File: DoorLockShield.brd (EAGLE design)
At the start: 160 x 100 mm, 1 part

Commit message: added schematic
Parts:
- added 24V: (no value), con-ptr500:AK500/2
- added C1: (no value), rcl:E7,5-16
- added FREI, L_V_T_N: (no value), con-phoenix-254:4POL254
- added IC2: 74HC595N, 74xx-eu:DIL16
- added L_V_T_O: (no value), con-phoenix-254:6POL254
- added RANDOM: (no value), con-phoenix-254:5POL254
- added RFID: (no value), con-phoenix-254:8POL254
- added RFID-LED: (no value), con-phoenix-254:3POL254
- added R_S_D, TT: (no value), con-phoenix-254:2POL254
- added SV1: (no value), con-lstb:MA03-1
- added SV2, SV3: (no value), con-lstb:MA08-1
- moved IC1 83.7 mm to (1.00, 6.08)
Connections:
- removed net +3V3: IC1.2
- new net 00: FREI.1, IC1.13
- new net 01: FREI.2, IC1.14
- new net 02: IC1.15, SV3.2
- new net 03: IC1.16, SV3.1
- new net 04: IC1.17
- new net 05: IC1.18, RFID.5
- new net 06: IC1.19
- new net 06_IN: RFID.4, SV1.2
- new net 07: IC1.20, IC2.14
- new net 08: IC1.21, IC2.12
- new net 09: IC1.22, IC2.11
- new net 10: IC1.23
- new net 11: IC1.24, RFID.3
- new net 12: IC1.25, RFID.2
- new net 13: IC1.26, RFID.1
- new net 1A: SV2.5
- new net 1B: SV2.6
- new net 24V: 24V.1, SV2.1
- new net 2A: SV2.4
- new net 2B: SV2.3
- new net 3.3V: IC1.2, RANDOM.3
- new net 5V: C1.+, IC1.6, IC2.10, IC2.16, L_V_T_N.3, L_V_T_O.4, RFID.6, SV1.3, SV2.7, SV3.6
- new net A0: IC1.7, L_V_T_O.2
- new net A1: IC1.8, R_S_D.2
- new net A2: L_V_T_O.1
- new net A3: IC1.10, TT.2
- new net A4: FREI.3, IC1.11
- new net A5: FREI.4, IC1.12
- new net AGND: C1.-, IC1.27, IC1.4, IC1.5, IC2.13, IC2.8, IC2.9, L_V_T_N.4, L_V_T_O.5, L_V_T_O.6, RFID.7, RFID.8, R_S_D.1, SV2.2, SV2.8, TT.1
- new net AREF: IC1.28, RANDOM.1
- new net N$1: SV1.1
- new net N$11: SV3.7
- new net N$13: SV3.5
- new net N$14: SV3.3, SV3.4
- new net N$6: IC2.7
- new net QA: IC2.15, RFID-LED.3
- new net QB: IC2.1, RFID-LED.2
- new net QC: IC2.2, RFID-LED.1
- new net QD: IC2.3, L_V_T_O.3
- new net QE: IC2.4, SV3.8
- new net QF: IC2.5, L_V_T_N.1
- new net QG: IC2.6, L_V_T_N.2
- new net RST: IC1.1, RANDOM.2
- net +5V: now also RANDOM.4
- net GND: now also 24V.2, RANDOM.5; no longer IC1.27, IC1.4, IC1.5
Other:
- board size 160 x 100 mm -> 70.6 x 65.4 mm

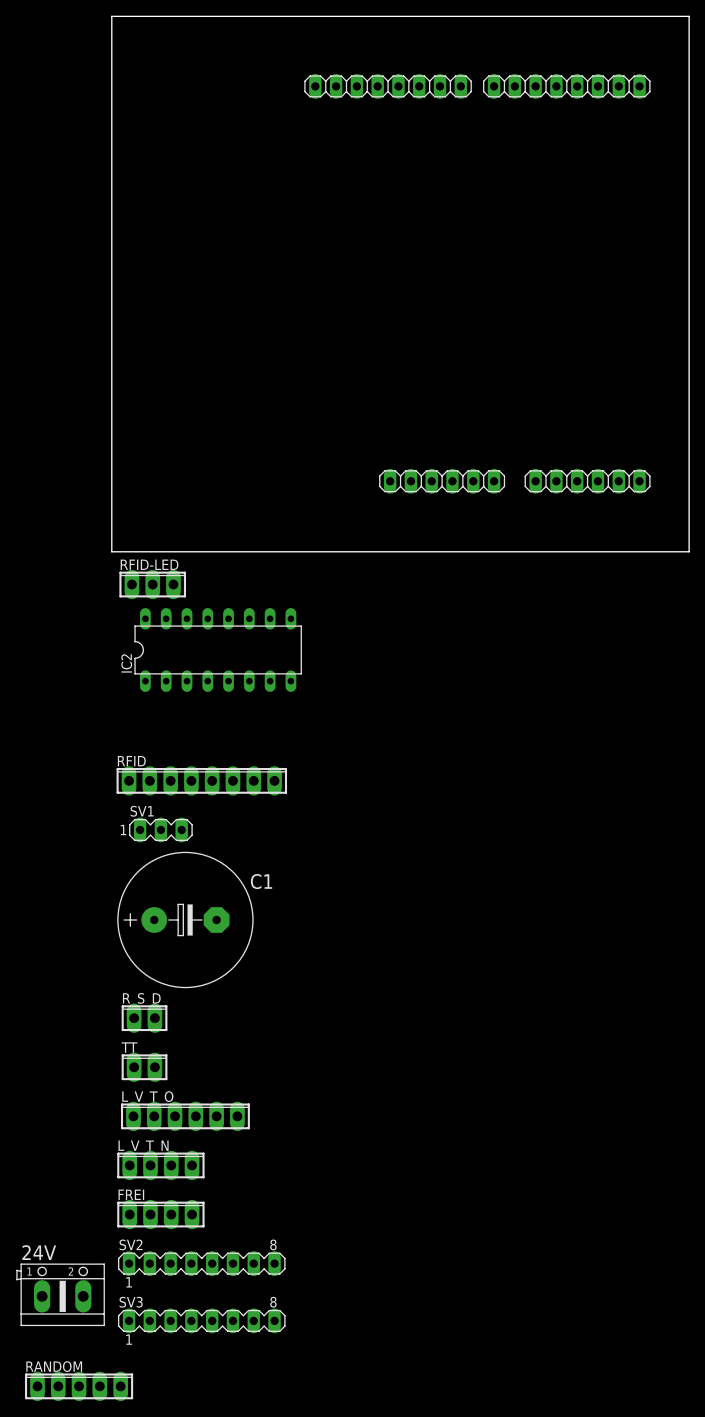
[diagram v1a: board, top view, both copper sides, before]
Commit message: finalized schematik
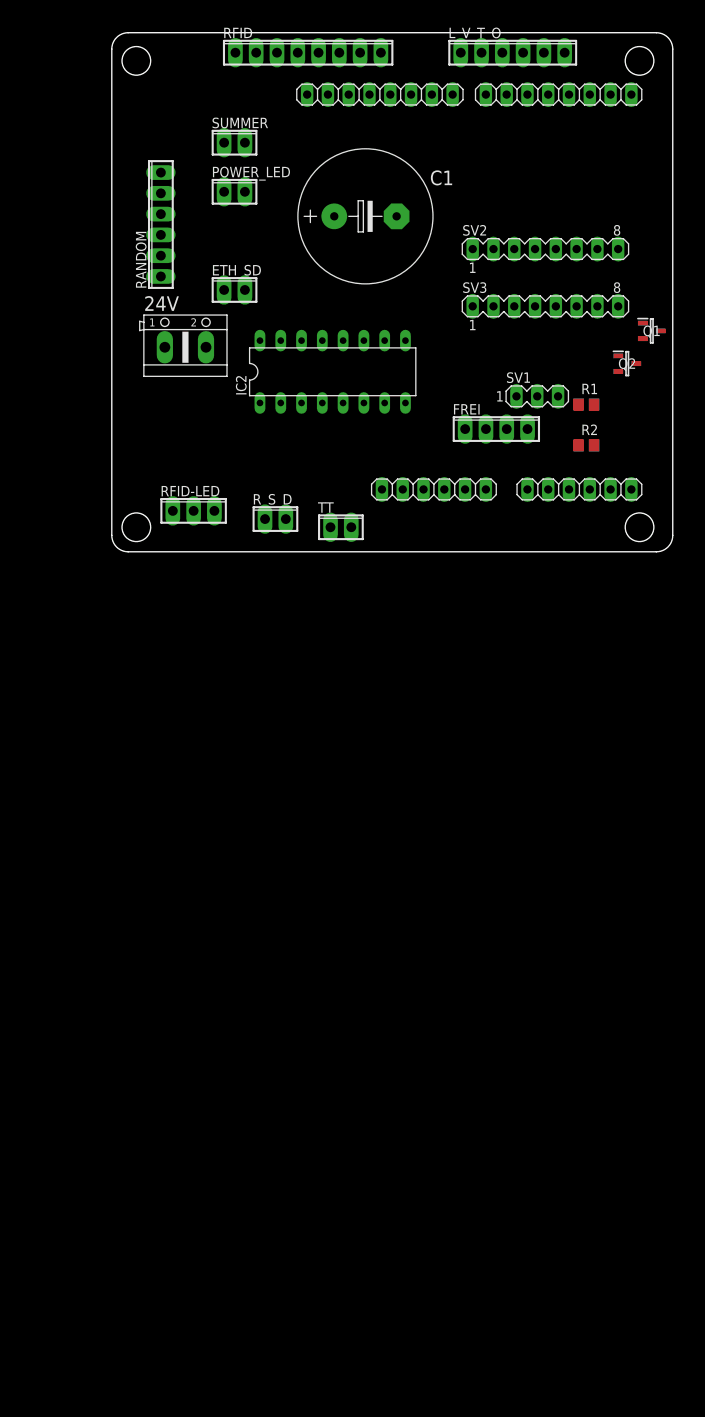
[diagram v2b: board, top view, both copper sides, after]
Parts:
- removed L_V_T_N: (no value), con-phoenix-254:4POL254
- added ETH_SD: (no value), con-phoenix-254:2POL254
- added POWER_LED, SUMMER: 1 is V & 2 is Gnd, con-phoenix-254:2POL254
- added Q1, Q2: FDN5632N-F085, FDN5632N-F085:SOT95P237X122-3N
- added R1, R2: 220 ohm, CommonParts:R0805
- RANDOM: device con-phoenix-254:5POL254 -> con-phoenix-254:6POL254
- moved RANDOM 142.4 mm to (6.00, 40.0), turned to 90 degrees
- moved L_V_T_O 136.0 mm to (49.0, 61.0)
- moved SV2 130.9 mm to (53.0, 37.0)
- moved SV3 130.9 mm to (53.0, 30.0)
- moved 24V 117.0 mm to (9.00, 25.0)
- moved FREI 104.4 mm to (47.0, 15.0)
- moved RFID 89.9 mm to (24.0, 61.0)
- moved C1 88.8 mm to (31.0, 41.0)
- moved TT 70.2 mm to (28.0, 3.00)
- moved SV1 70.2 mm to (52.0, 19.0)
- moved R_S_D 63.1 mm to (20.0, 4.00)
- moved IC2 36.8 mm to (27.0, 22.0)
- moved RFID-LED 10.3 mm to (10.0, 5.00)
- moved IC1 1.41 mm to (0.00, 5.08)
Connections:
- new net N$2: Q2.1, R1.2
- new net N$3: Q1.1, R2.2
- new net N$4: POWER_LED.2, Q1.3
- new net N$5: Q2.3, SUMMER.2
- net 04: now also ETH_SD.2
- net 10: now also ETH_SD.1
- net 5V: now also L_V_T_O.5, POWER_LED.1, SUMMER.1; no longer L_V_T_N.3
- net A2: now also IC1.9
- net AGND: now also Q1.2, Q2.2; no longer L_V_T_N.4, L_V_T_O.5
- net GND: now also RANDOM.6
- net QF: now also R1.1; no longer L_V_T_N.1
- net QG: now also R2.1; no longer L_V_T_N.2
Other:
- board size 70.6 x 65.4 mm -> 68.6 x 63.4 mm

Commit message: started to add brd
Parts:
- removed L_V_T_O: (no value), con-phoenix-254:6POL254
- removed R_S_D, TT: (no value), con-phoenix-254:2POL254
- added L_TÜR: (no value), con-phoenix-254:6POL254
- added R_TÜR, TÜR_TER.: (no value), con-phoenix-254:2POL254
- FREI: device con-phoenix-254:4POL254 -> con-phoenix-254:6POL254
- moved RANDOM 60.6 mm to (63.5, 21.0), turned to 270 degrees
- moved Q2 51.0 mm to (18.0, 47.0), flipped to the bottom
- moved Q1 50.0 mm to (18.0, 41.0), flipped to the bottom
- moved R2 49.5 mm to (23.0, 48.0), flipped to the bottom
- moved RFID 45.2 mm to (5.00, 20.0), turned to 90 degrees
- moved R1 42.4 mm to (23.0, 42.0), flipped to the bottom
- moved RFID-LED 30.9 mm to (5.00, 35.5), turned to 90 degrees
- moved FREI 27.9 mm to (63.5, 37.5), turned to 270 degrees
- moved SV3 27.8 mm to (27.5, 19.0), turned to 180 degrees
- moved ETH_SD 27.1 mm to (17.0, 5.00), turned to 180 degrees
- moved SV2 26.2 mm to (27.5, 31.2)
- moved 24V 25.9 mm to (25.5, 5.00), turned to 180 degrees
- moved IC2 23.1 mm to (38.5, 42.0)
- moved C1 23.0 mm to (48.0, 25.5), turned to 90 degrees
- moved SV1 14.5 mm to (39.0, 12.5)
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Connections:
- removed net GND: 24V.2, RANDOM.5, RANDOM.6
- new net GND24: 24V.2, SV2.2
- net 5V: now also FREI.5, L_TÜR.4, L_TÜR.5; no longer L_V_T_O.4, L_V_T_O.5
- net A0: now also L_TÜR.2; no longer L_V_T_O.2
- net A1: now also R_TÜR.2; no longer R_S_D.2
- net A2: now also L_TÜR.1; no longer L_V_T_O.1
- net A3: now also TÜR_TER..2; no longer TT.2
- net AGND: now also FREI.6, L_TÜR.6, RANDOM.5, RANDOM.6, R_TÜR.1, TÜR_TER..1; no longer L_V_T_O.6, R_S_D.1, SV2.2, TT.1
- net N$2: now also Q1.1; no longer Q2.1
- net N$3: now also Q2.1; no longer Q1.1
- net N$4: now also Q2.3; no longer Q1.3
- net N$5: now also Q1.3; no longer Q2.3
- net QD: now also L_TÜR.3; no longer L_V_T_O.3
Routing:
- net 24V: track 0.00 -> 40.8 mm
- net GND24: track 0.00 -> 38.4 mm, vias 0 -> 1
- net 5V: track 0.00 -> 32.0 mm
- net N$4: track 0.00 -> 13.9 mm
- net N$5: track 0.00 -> 13.5 mm
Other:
- board size 68.6 x 63.4 mm -> 69 x 63 mm
- board text added: "G"
- board text added: "V"

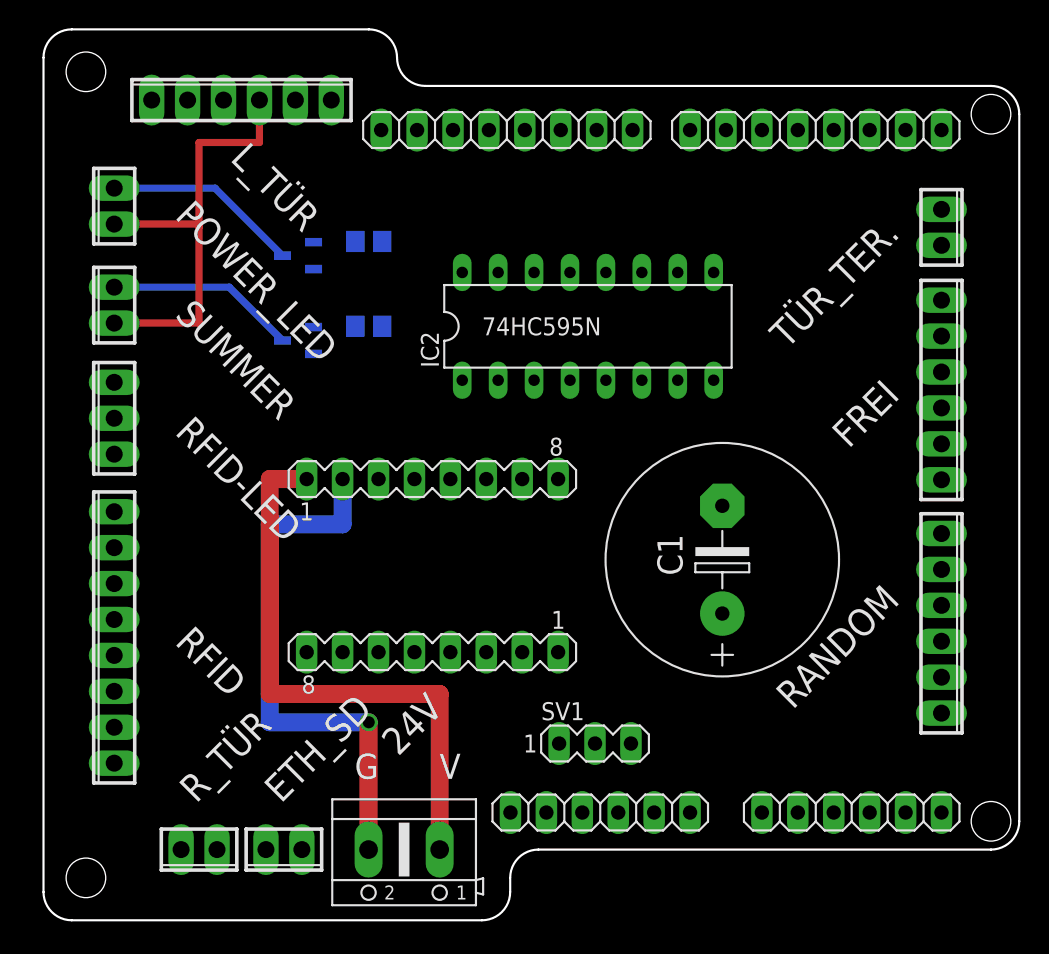
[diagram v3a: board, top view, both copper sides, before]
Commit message: added description names on sch and brd
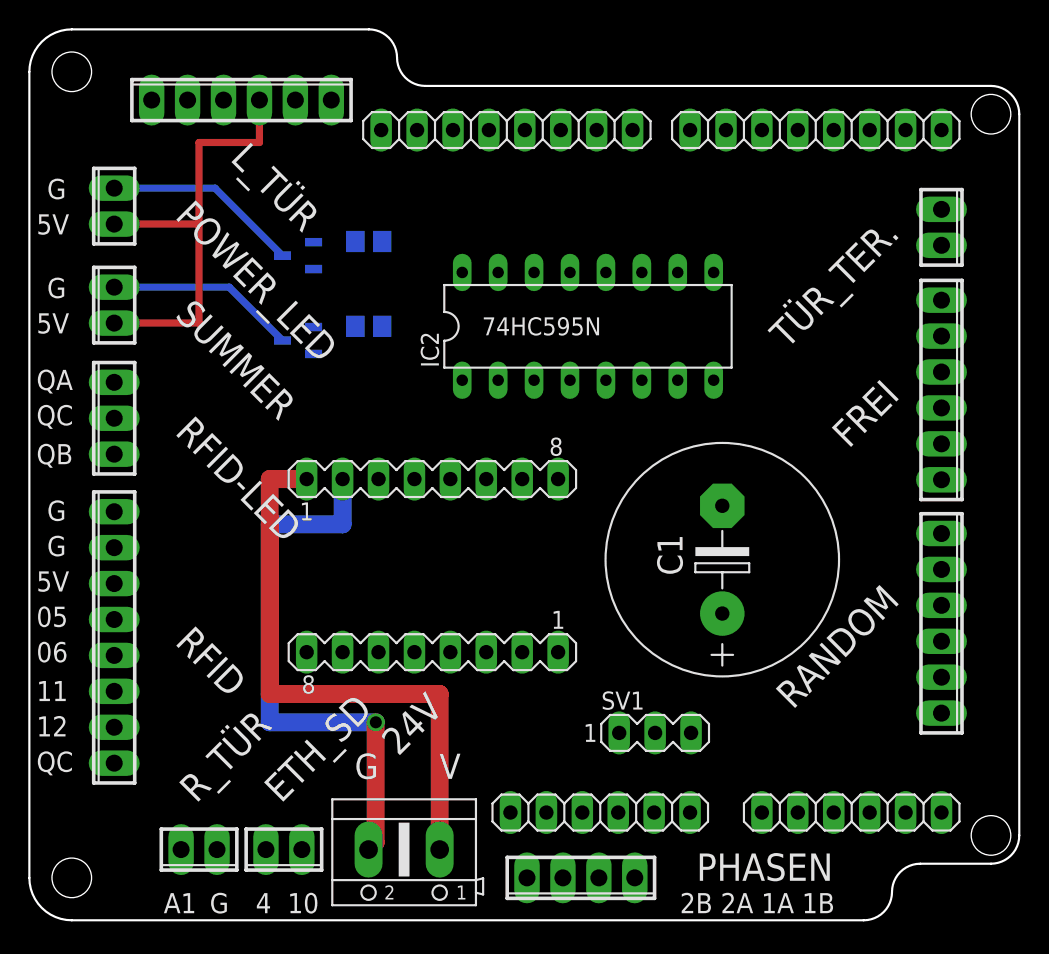
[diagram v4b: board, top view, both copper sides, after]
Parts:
- added PHASEN: (no value), con-phoenix-254:4POL254
- C1: value (none) -> 470uF
- moved SV1 4.32 mm to (43.2, 13.2)
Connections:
- net 02 renamed STEP
- net 03 renamed DIR
- net 04 renamed SS_SD
- net 05 renamed ROT_2_SCHWARZ_G_A
- net 07 renamed SER
- net 08 renamed RCK
- net 09 renamed SCK
- net 10 renamed ETHERNET
- net 11 renamed ROT_2_SCHWARZ_K_A
- net 12 renamed ROT_1_SCHWARZ
- net 13 renamed GRÜN_1_SCHWARZ
- net 3.3V renamed 3.3V_OUT
- net A0 renamed SCHLIESS_Z_TÜR
- net A1 renamed R_SCHALTER_TÜR
- net A2 renamed TÜR_ZU_SCHALTER
- net A3 renamed TERRASSENTÜR
- net QA renamed LED1_2_GRAUE_S
- net QB renamed LED2_1_GRAU_S
- net QC renamed LED3_GRAU
- net QD renamed RELAIS_SUMMER
- net QE renamed ENABLE
- net QF renamed SUMMER
- net QG renamed POWER_LED
- removed net 06: IC1.19
- removed net N$1: SV1.1
- removed net N$11: SV3.7
- removed net N$13: SV3.5
- removed net N$6: IC2.7
- new net JUMPER_SS: IC1.19, SV1.1
- new net QH: FREI.6, IC2.7
- net 1A: now also PHASEN.2
- net 1B: now also PHASEN.1
- net 2A: now also PHASEN.3
- net 2B: now also PHASEN.4
- net AGND: no longer FREI.6
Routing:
- net GND24: track 38.4 -> 39.1 mm
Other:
- board size 69 x 63 mm -> 70 x 63 mm
- board text added: "05"
- board text added: "06"
- board text added: "10"
- board text added: "11"
- board text added: "12"
- board text added: "2B 2A 1A 1B"
- board text added: "4"
- board text added: "5V"
- board text added: "A1"
- board text added: "QA"
- board text added: "QB"
- board text added: "QC"

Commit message: small design change in brd
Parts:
- moved ETH_SD 1.00 mm to (16.0, 5.00)
- moved L_TÜR 1.00 mm to (13.0, 58.0)
- moved R_TÜR 1.00 mm to (10.0, 5.00)
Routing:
- net 5V: track 32.0 -> 31.0 mm

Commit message: final boeard has to be reviewed
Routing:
- net AGND: track 0.00 -> 224.9 mm, vias 0 -> 1
- net 5V: track 31.0 -> 235.1 mm, vias 0 -> 3
- net SCHLIESS_Z_TÜR: track 0.00 -> 140.2 mm, vias 0 -> 4
- net SS_SD: track 0.00 -> 104.1 mm, vias 0 -> 2
- net TÜR_ZU_SCHALTER: track 0.00 -> 97.7 mm, vias 0 -> 4
- net R_SCHALTER_TÜR: track 0.00 -> 88.2 mm, vias 0 -> 6
- net ETHERNET: track 0.00 -> 84.7 mm, vias 0 -> 4
- net ROT_2_SCHWARZ_K_A: track 0.00 -> 83.8 mm
- net ROT_1_SCHWARZ: track 0.00 -> 81.9 mm, vias 0 -> 2
- net ROT_2_SCHWARZ_G_A: track 0.00 -> 80.5 mm, vias 0 -> 3
- net GRÜN_1_SCHWARZ: track 0.00 -> 71.6 mm, vias 0 -> 4
- net AREF: track 0.00 -> 66.8 mm, vias 0 -> 4
- net JUMPER_SS: track 0.00 -> 60.6 mm, vias 0 -> 2
- net STEP: track 0.00 -> 57.5 mm
- net 06_IN: track 0.00 -> 47.9 mm, vias 0 -> 3
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- added copper zone on layer 1, net AGND
- added copper zone on layer 16, net AGND
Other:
- board size 70 x 63 mm -> 81 x 63 mm
- board text added: "01"
- board text added: "3.3V"
- board text added: "A0"
- board text added: "A2"
- board text added: "A4"
- board text added: "A5"
- board text added: "AREF"
- board text added: "For infos about Names on the clambs scan the barcode or look in our git"
- board text added: "Made by Moritz for Freilab"
- board text added: "QD"
- board text added: "QH"
- board text added: "RST"
